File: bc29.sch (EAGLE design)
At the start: 107 parts, among them IC1 TSC900BIJA, IC10 MC14516B, IC11 CD4070B, IC12 MC14516B, IC13 CD4013, IC14 CD4023, IC15 CD4013B, IC16 MC14073B, IC17 CD4070B, IC18 LP2951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

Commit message: Incorperate display module knowldge
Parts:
- removed J1: 2520-5, con-3m:2520-5
- added J2: 2520-5, con-3m:2520-5
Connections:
- removed net !DOWN: IC10A.U/!D, IC11C.O, IC11D.I1, IC12A.U/!D, IC14B.I1, IC16C.I0, IC5B.I1, J1-1.KL
- removed net !LCD_RESET: IC3A.Z, J1-17.KL
- removed net !UP_DOWN_CLK: IC11A.O, IC14C.I0, IC9B.I1, J1-15.KL
- removed net AH_NEGATIVE_LCD: IC11C.I1, IC8C.I1, IC9A.I1, IC9D.O, J1-18.KL
- removed net LCD-13: IC14A.O, IC19B.I0, J1-13.KL
- removed net LCD-16: IC15A.D, IC9A.O, IC9D.I0, J1-16.KL
- removed net LCD-3: C20.1, IC19B.I1, J1-3.KL
- removed net LCD_45_HZ: IC17A.I1, IC17B.I0, IC17C.I1, IC17D.I0, J1-19.KL
- removed net V_F_OUT: D7.C, E1.-, J1-20.KL
- new net !IN_LED: IC11C.I1, IC8C.I1, IC9A.I1, IC9D.O, J2-18.KL
- new net !LCD_COUNTER_BACKPLANE: IC17A.I1, IC17B.I0, IC17C.I1, IC17D.I0, J2-19.KL
- new net !LCD_COUNTER_CARRY: C20.1, IC19B.I1, J2-3.KL
- new net !LCD_COUNTER_CLK: IC11A.O, IC14C.I0, IC9B.I1, J2-15.KL
- new net !LCD_COUNTER_RESET: IC3A.Z, J2-17.KL
- new net !OUT_LED: IC15A.D, IC9A.O, IC9D.I0, J2-16.KL
- new net LCD_COUNTER_BLANK: IC16C.O, J2-9.KL
- new net LCD_COUNTER_ENABLE: IC14A.O, IC19B.I0, J2-13.KL
- new net LCD_COUNTER_UP: IC10A.U/!D, IC11C.O, IC11D.I1, IC12A.U/!D, IC14B.I1, IC16C.I0, IC5B.I1, J2-1.KL
- new net LED_ANODE: D7.C, E1.-, J2-20.KL
- net +5V: now also J2-14.KL; no longer J1-14.KL
- net 12+: now also J2-4.KL; no longer J1-4.KL
- net 12-: now also J2-2.KL; no longer J1-2.KL
- net GND: now also J2-5.KL; no longer J1-5.KL
- net LCD_COLON: now also J2-11.KL; no longer J1-11.KL
- net LCD_DECIMAL_POINT: now also J2-7.KL; no longer J1-7.KL
- net LCD_MINUS_SIGN: now also J2-8.KL; no longer J1-8.KL
- net LCD_ONE_MSD: now also J2-10.KL; no longer J1-10.KL
- net OVER_FLOW_UP: no longer IC16C.O, J1-9.KL
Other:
- note added: "45Hz Square Wave +5VDC/GND"
- note removed: "Blanks 4 LSD"
- note removed: "Count Zero"
- note removed: "Overflow?"
- note removed: "Up/Down Counter"
- moved on the sheet: D7, E1, IC10, IC11A, IC11C, IC12, IC13B, IC14A, IC14B, IC14C, IC16C, IC8A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

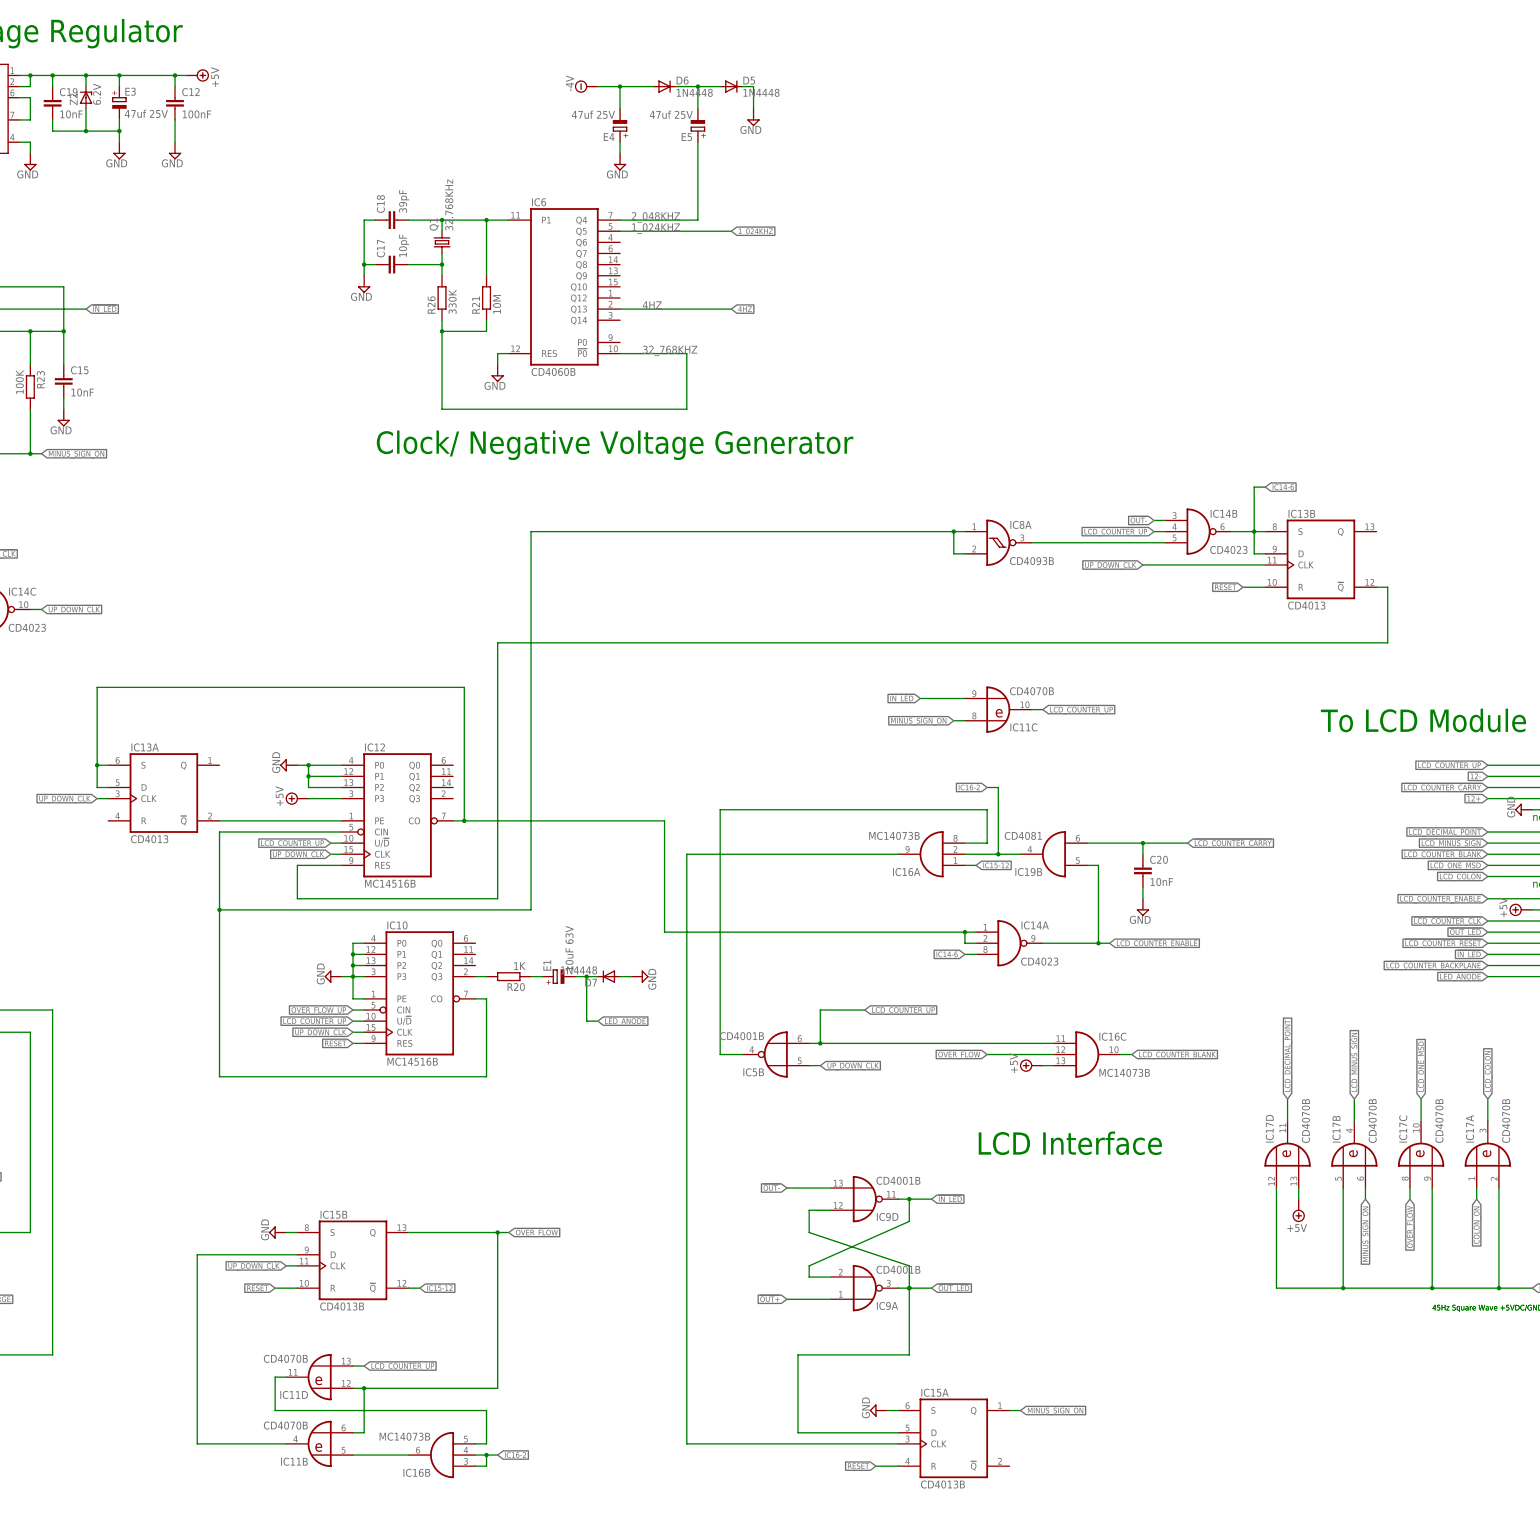
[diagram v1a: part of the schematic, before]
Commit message: Move things around. Update png files
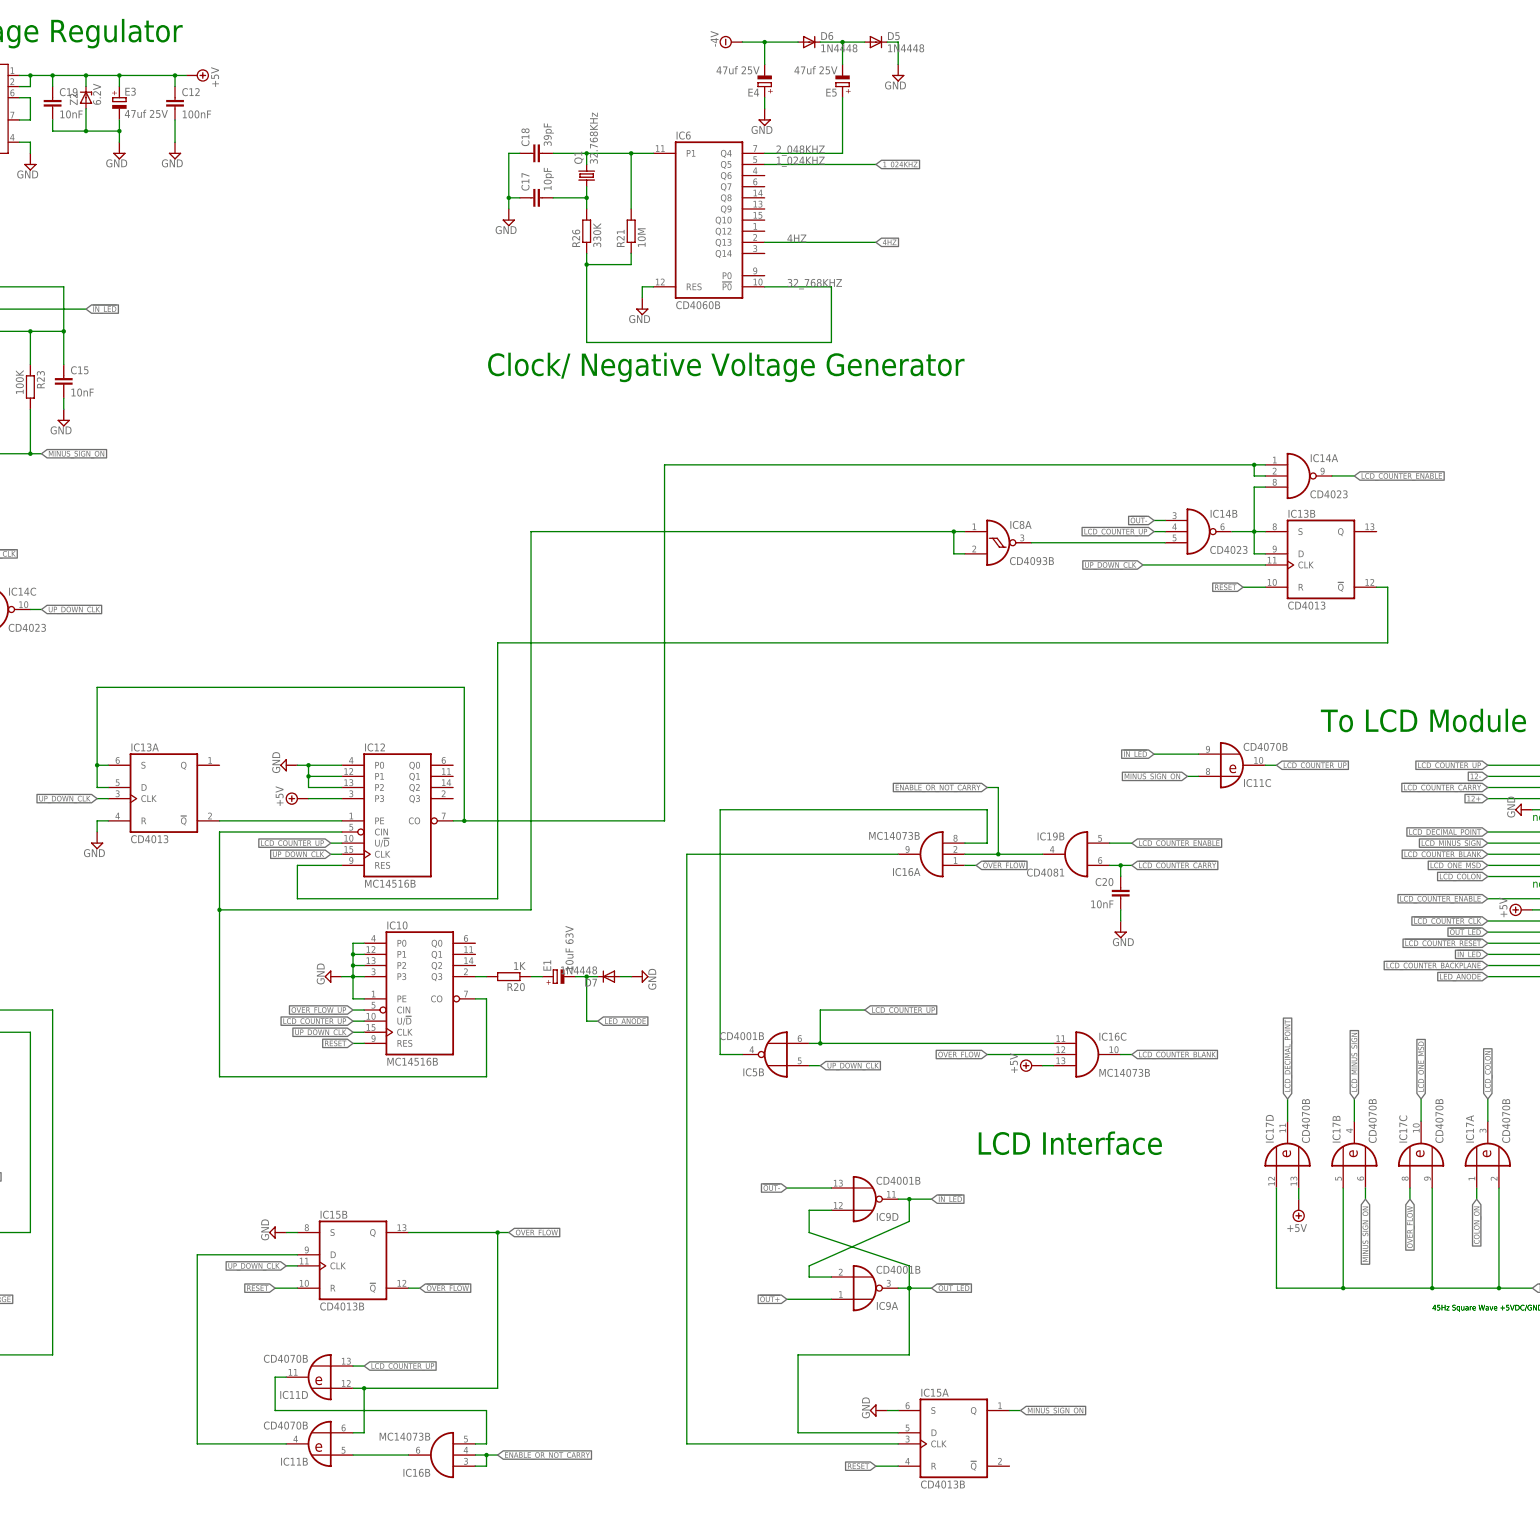
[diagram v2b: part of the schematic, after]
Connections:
- net IC15-12 renamed !OVER_FLOW
- net IC16-2 renamed ENABLE_OR_NOT_CARRY
- net GND: now also IC13A.R
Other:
- moved on the sheet: C17, C18, C20, D5, D6, E4, E5, IC11C, IC14A, IC19B, IC6, Q1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

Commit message: Clean up net names
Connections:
- net !LCD_COUNTER_BACKPLANE renamed LCD_COUNTER_BACKPLANE
- net !LCD_COUNTER_CLK renamed LCD_COUNTER_CLK
- removed net IC17-1: IC9B.O, IC9C.I1
- net COLON_ON: now also IC9B.O, IC9C.I1
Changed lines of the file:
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@@
 <?xml version="1.0" encoding="utf-8"?>
 <!DOCTYPE eagle SYSTEM "eagle.dtd">
-<eagle version="7.1.0">
+<eagle version="7.2.0">
 <drawing>
 <settings>
@@
 <setting verticaltext="up"/>
 </settings>
-<grid distance="0.1" unitdist="inch" unit="inch" style="lines" multiple="1" display="yes" altdistance="0.01" altunitdist="inch" altunit="inch"/>
+<grid distance="0.1" unitdist="inch" unit="inch" style="lines" multiple="1" display="no" altdistance="0.01" altunitdist="inch" altunit="inch"/>
 <layers>
 <layer number="1" name="Top" color="4" fill="1" visible="no" active="no"/>
@@
 </segment>
 </net>
-<net name="IC17-1" class="0">
-<segment>
-<pinref part="IC9" gate="C" pin="I1"/>
-<wire x1="38.1" y1="35.56" x2="38.1" y2="22.86" width="0.1524" layer="91"/>
-<wire x1="83.82" y1="35.56" x2="86.36" y2="35.56" width="0.1524" layer="91"/>
-<label x="86.36" y="35.56" size="1.27" layer="95" xref="yes"/>
-<wire x1="38.1" y1="22.86" x2="83.82" y2="22.86" width="0.1524" layer="91"/>
-<wire x1="83.82" y1="22.86" x2="83.82" y2="35.56" width="0.1524" layer="91"/>
-<pinref part="IC9" gate="B" pin="O"/>
-<wire x1="83.82" y1="35.56" x2="76.2" y2="35.56" width="0.1524" layer="91"/>
-<junction x="83.82" y="35.56"/>
-</segment>
-</net>
 <net name="N$25" class="0">
 <segment>
@@
 <label x="439.42" y="-68.58" size="1.27" layer="95" rot="R270" xref="yes"/>
 </segment>
+<segment>
+<pinref part="IC9" gate="C" pin="I1"/>
+<wire x1="38.1" y1="35.56" x2="38.1" y2="22.86" width="0.1524" layer="91"/>
+<wire x1="83.82" y1="35.56" x2="86.36" y2="35.56" width="0.1524" layer="91"/>
+<label x="86.36" y="35.56" size="1.27" layer="95" xref="yes"/>
+<wire x1="38.1" y1="22.86" x2="83.82" y2="22.86" width="0.1524" layer="91"/>
+<wire x1="83.82" y1="22.86" x2="83.82" y2="35.56" width="0.1524" layer="91"/>
+<pinref part="IC9" gate="B" pin="O"/>
+<wire x1="83.82" y1="35.56" x2="76.2" y2="35.56" width="0.1524" layer="91"/>
+<junction x="83.82" y="35.56"/>
+</segment>
 </net>
 <net name="!LCD_COUNTER_CARRY" class="0">
@@
 </segment>
 </net>
-<net name="!LCD_COUNTER_BACKPLANE" class="0">
+<net name="LCD_COUNTER_BACKPLANE" class="0">
 <segment>
 <pinref part="J2" gate="-19" pin="KL"/>
@@
 </segment>
 </net>
-<net name="!LCD_COUNTER_CLK" class="0">
+<net name="LCD_COUNTER_CLK" class="0">
 <segment>
 <pinref part="J2" gate="-15" pin="KL"/>

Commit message: Clean up some net names
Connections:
- net N$20 renamed !CHARGE
- net N$21 renamed !DISCHARGE
- net N$53 renamed D_CHARGE
- net N$55 renamed NEG_COMPARATOR
- net N$56 renamed POS_COMPARATOR
- net N$57 renamed D_DISCHARGE
- net OUT renamed OP_AMP__OUT
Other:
- moved on the sheet: C11, IC5C, IC7A, IC7B, IC8D, IC9B, R17

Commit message: Rference files on Yahoo Solectria_EV site
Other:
- note added: "Reset"
- moved on the sheet: C17, C18, C20, D5, D6, D7, E1, E4, E5, IC10, IC11B, IC11C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
